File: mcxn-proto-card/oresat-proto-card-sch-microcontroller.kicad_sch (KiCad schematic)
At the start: 102 parts, among them J9 SM14B-SHLS-TF, U1 MCXN947VKLT, U8 TCAN330, Y2 24 MHz

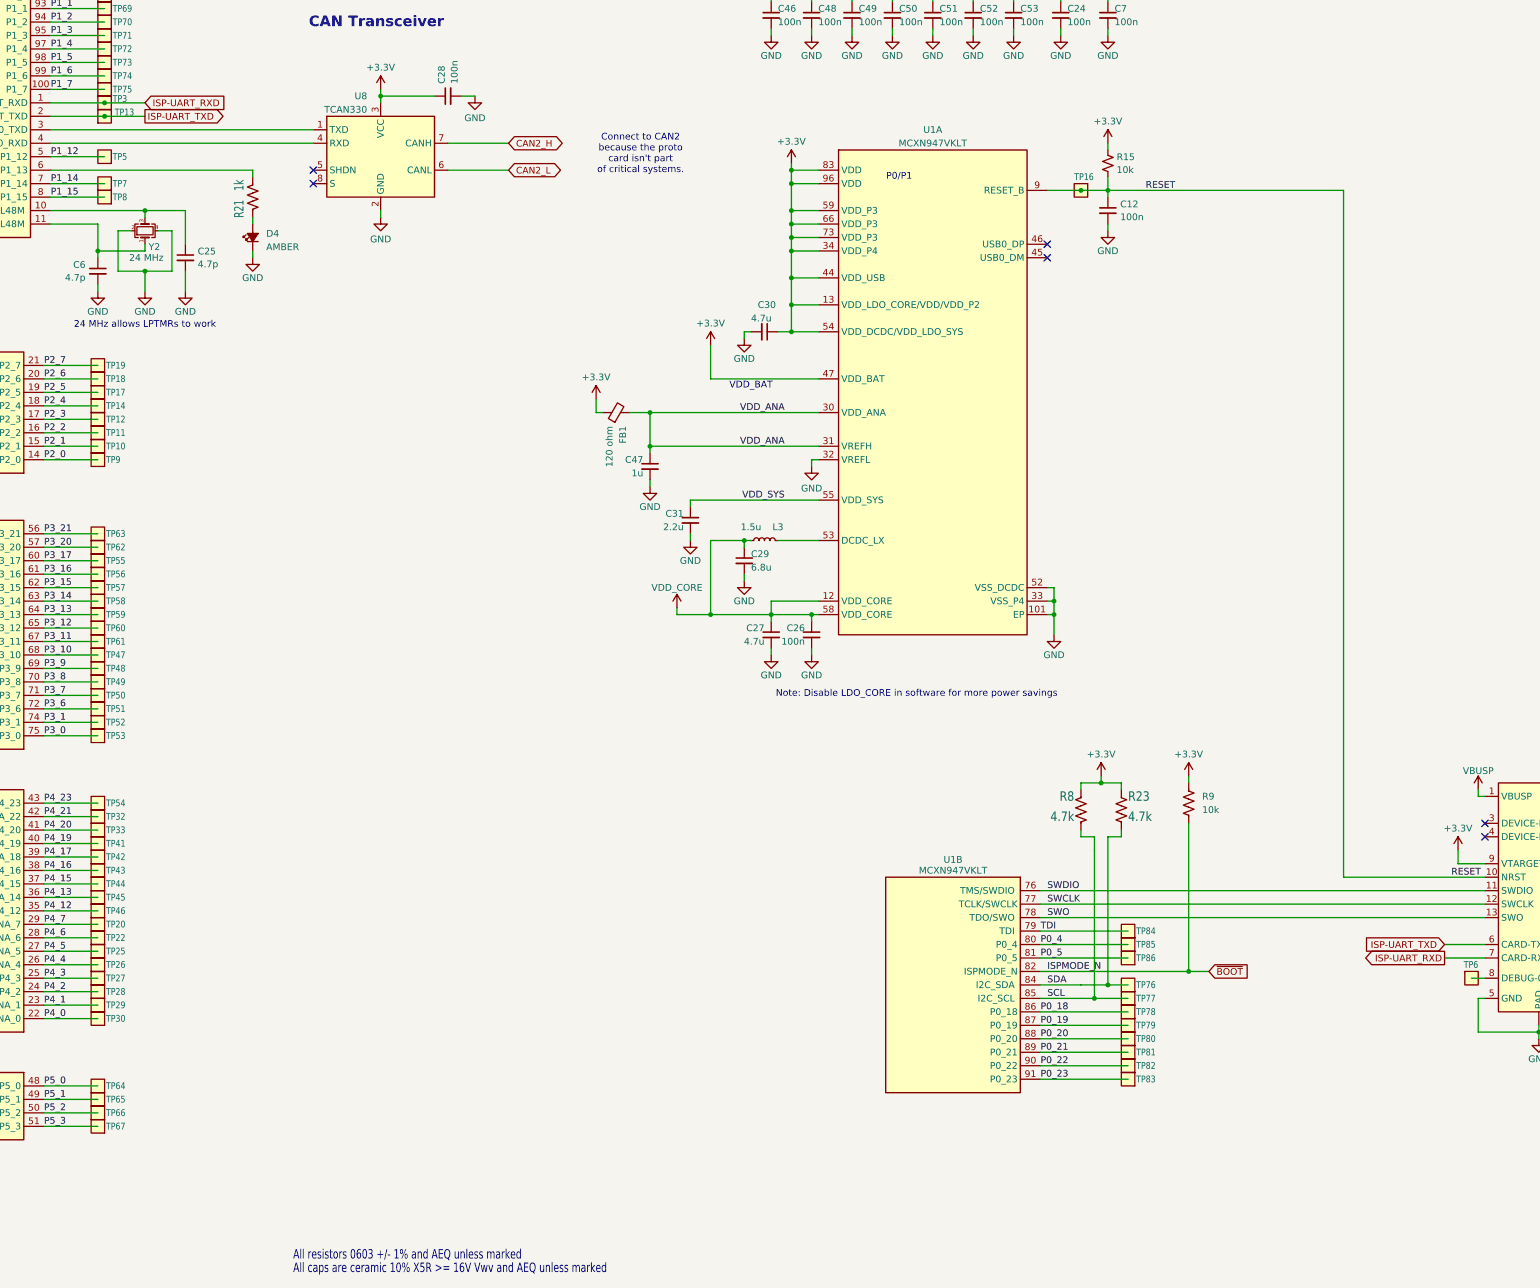
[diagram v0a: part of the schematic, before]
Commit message: Final MCXN protocard cleanup
Made schematic fancy with hierarchical pins, cleaned up schematics a bit, and fixed silk screen a ton. Ready for fab.
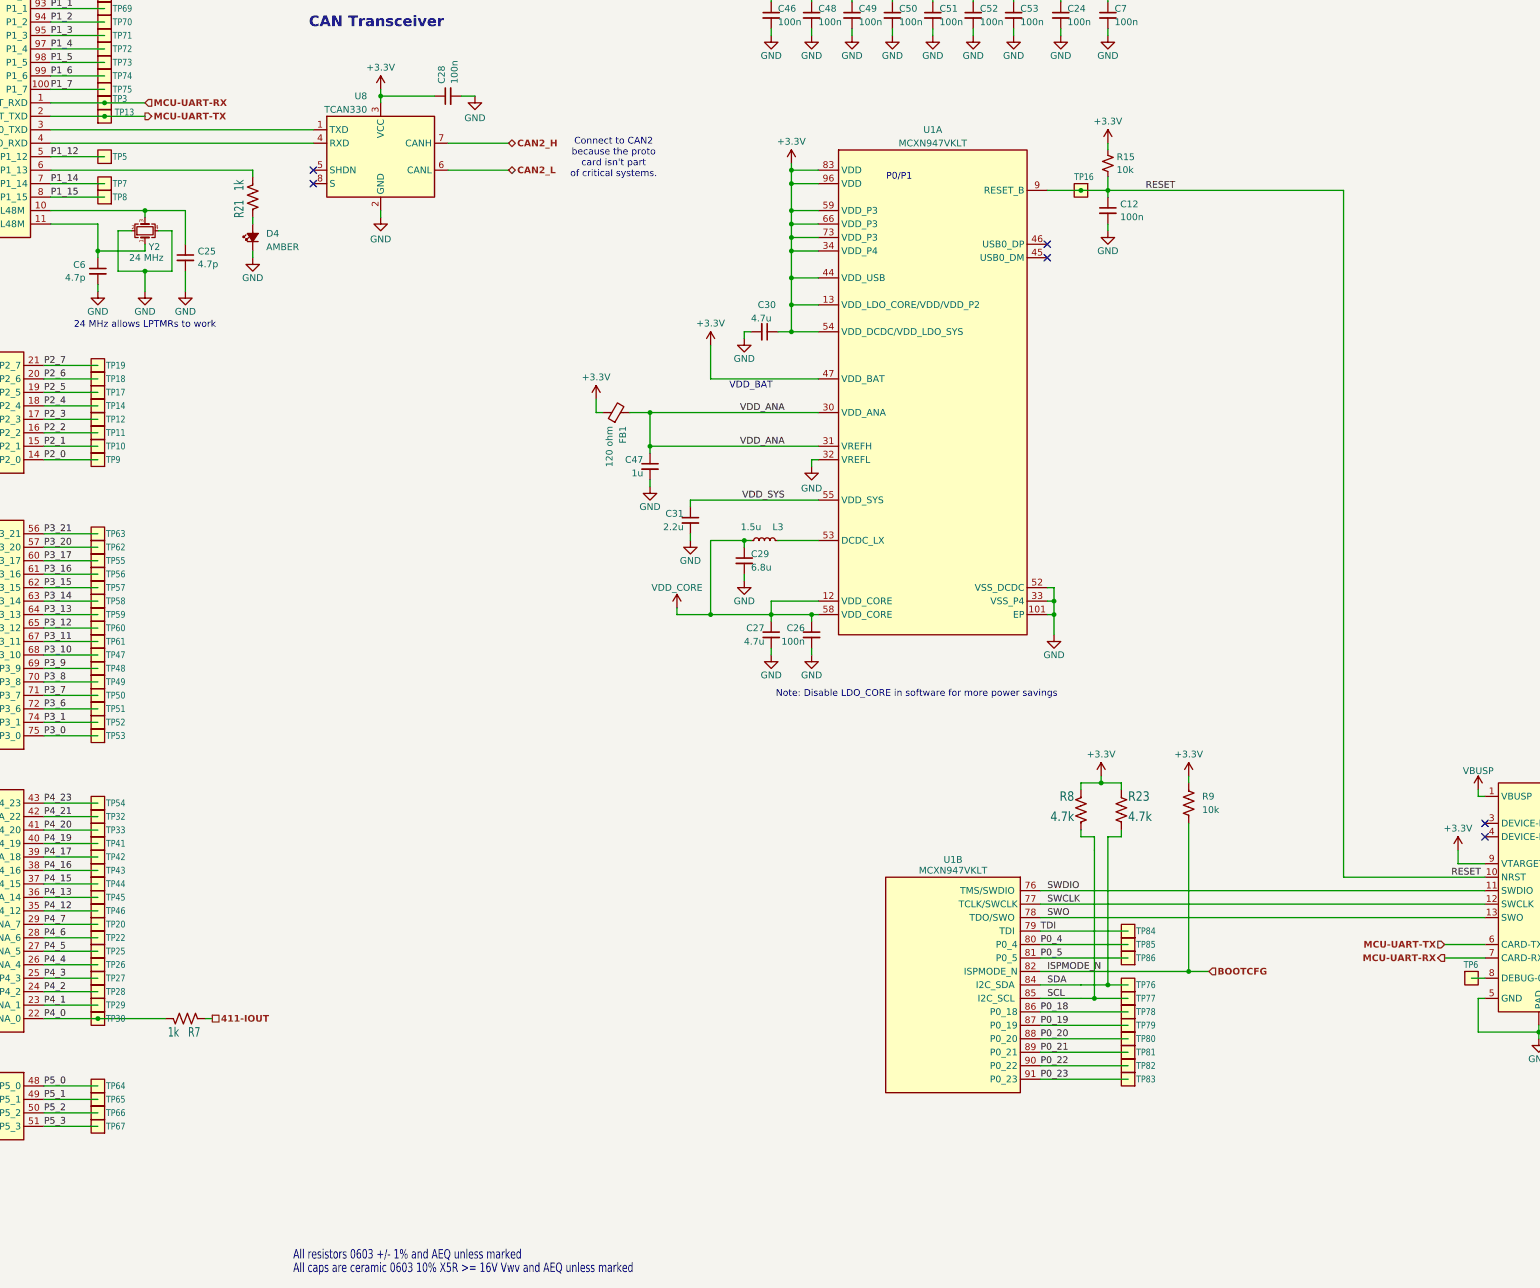
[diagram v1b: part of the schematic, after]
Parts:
- added R7: 1k, oresat-passives:0603-C-NOSILK, symbol Device:R_US
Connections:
- net P4_0: now also R7.1
- net ISP-UART_RXD renamed MCU-UART-RX
- net ISP-UART_TXD renamed MCU-UART-TX
- net ~{BOOT} renamed BOOTCFG
- new net 411-IOUT: R7.2
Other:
- note added: "All caps are ceramic 0603 10% X5R >= 16V Vwv and AEQ unless marked"
- note removed: "All caps are ceramic 10% X5R >= 16V Vwv and AEQ unless marked"
- company: (none) -> Portland State Aerospace Society
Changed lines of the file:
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@@
 	(title_block
 		(title "OreSat MCXN Proto Card")
-		(date "2025-11-13")
+		(date "2025-12-28")
 		(rev "6.0")
+		(company "Portland State Aerospace Society")
 	)
 	(text "Connect to CAN2 \nbecause the proto\ncard isn't part \nof critical systems."
 		(exclude_from_sim no)
-		(at 178.562 55.372 0)
+		(at 173.482 56.134 0)
 		(effects
 			(font
@@
 		)
 	)
-	(text "All caps are ceramic 10% X5R >= 16V Vwv and AEQ unless marked"
+	(text "All caps are ceramic 0603 10% X5R >= 16V Vwv and AEQ unless marked"
 		(exclude_from_sim no)
 		(at 113.03 266.7 0)
@@
 	)
 	(junction
+		(at 76.2 218.44)
+		(diameter 0)
+		(color 0 0 0 0)
+	)
+	(junction
 		(at 129.54 44.45)
 		(diameter 0)
@@
 	(wire
 		(pts
+			(xy 76.2 218.44) (xy 88.9 218.44)
+		)
+		(stroke
+			(width 0)
+			(type default)
+		)
+	)
+	(wire
+		(pts
 			(xy 269.24 173.99) (xy 265.43 173.99)
 		)
@@
 		)
 	)
+	(wire
+		(pts
+			(xy 96.52 218.44) (xy 97.79 218.44)
+		)
+		(stroke
+			(width 0)
+			(type default)
+		)
+	)
 	(label "P3_13"
 		(at 66.04 142.24 0)
@@
 		)
 	)
-	(global_label "ISP-UART_TXD"
-		(shape output)
-		(at 85.09 48.26 0)
-		(fields_autoplaced yes)
+	(hierarchical_label "BOOTCFG"
+		(shape input)
+		(at 285.75 209.55 0)
 		(effects
 			(font
 				(size 1.27 1.27)
+				(thickness 0.254)
+				(bold yes)
 			)
 			(justify left)
 		)
-		(property "Intersheetrefs" "${INTERSHEET_REFS}"
-			(at 101.8033 48.26 0)
-			(effects
-				(font
-					(size 1.27 1.27)
-				)
-				(justify left)
-			)
-		)
 	)
-	(global_label "CAN2_L"
-		(shape bidirectional)
-		(at 153.67 58.42 0)
-		(fields_autoplaced yes)
+	(hierarchical_label "MCU-UART-TX"
+		(shape output)
+		(at 85.09 48.26 0)
 		(effects
 			(font
-				(size 1.2446 1.2446)
+				(size 1.27 1.27)
+				(thickness 0.254)
+				(bold yes)
 			)
 			(justify left)
 		)
-		(property "Intersheetrefs" "${INTERSHEET_REFS}"
-			(at 164.4406 58.42 0)
-			(effects
-				(font
-					(size 1.27 1.27)
-				)
-				(justify left)
-			)
-		)
 	)
-	(global_label "ISP-UART_TXD"
-		(shape input)
-		(at 330.2 204.47 180)
-		(fields_autoplaced yes)
+	(hierarchical_label "CAN2_L"
+		(shape bidirectional)
+		(at 153.67 58.42 0)
 		(effects
 			(font
 				(size 1.27 1.27)
+				(thickness 0.254)
+				(bold yes)
 			)
-			(justify right)
-		)
-		(property "Intersheetrefs" "${INTERSHEET_REFS}"
-			(at 313.4867 204.47 0)
-			(effects
-				(font
-					(size 1.27 1.27)
-				)
-				(justify right)
-			)
+			(justify left)
 		)
 	)
-	(global_label "~{BOOT}"
-		(shape input)
-		(at 285.75 209.55 0)
-		(fields_autoplaced yes)
+	(hierarchical_label "CAN2_H"
+		(shape bidirectional)
+		(at 153.67 53.34 0)
 		(effects
 			(font
 				(size 1.27 1.27)
+				(thickness 0.254)
+				(bold yes)
 			)
 			(justify left)
 		)
-		(property "Intersheetrefs" "${INTERSHEET_REFS}"
-			(at 293.6338 209.55 0)
-			(effects
-				(font
-					(size 1.27 1.27)
-				)
-				(justify left)
-			)
-		)
 	)
-	(global_label "ISP-UART_RXD"
+	(hierarchical_label "MCU-UART-RX"
 		(shape input)
 		(at 85.09 45.72 0)
-		(fields_autoplaced yes)
 		(effects
 			(font
 				(size 1.27 1.27)
+				(thickness 0.254)
+				(bold yes)
 			)
 			(justify left)
 		)
-		(property "Intersheetrefs" "${INTERSHEET_REFS}"
-			(at 102.1057 45.72 0)
-			(effects
-				(font
-					(size 1.27 1.27)
-				)
-				(justify left)
-			)
-		)
 	)
-	(global_label "ISP-UART_RXD"
-		(shape output)
-		(at 330.2 207.01 180)
-		(fields_autoplaced yes)
+	(hierarchical_label "MCU-UART-TX"
+		(shape input)
+		(at 330.2 204.47 180)
 		(effects
 			(font
 				(size 1.27 1.27)
+				(thickness 0.254)
+				(bold yes)
 			)
 			(justify right)
 		)
-		(property "Intersheetrefs" "${INTERSHEET_REFS}"
-			(at 313.1843 207.01 0)
-			(effects
-				(font
-					(size 1.27 1.27)
-				)
-				(justify right)
-			)
-		)
 	)
-	(global_label "CAN2_H"
-		(shape bidirectional)
-		(at 153.67 53.34 0)
-		(fields_autoplaced yes)
+	(hierarchical_label "411-IOUT"
+		(shape passive)
+		(at 97.79 218.44 0)
 		(effects
 			(font
-				(size 1.2446 1.2446)
+				(size 1.27 1.27)
+				(thickness 0.254)
+				(bold yes)
 			)
 			(justify left)
 		)
-		(property "Intersheetrefs" "${INTERSHEET_REFS}"
-			(at 164.737 53.34 0)
-			(effects
-				(font
-					(size 1.27 1.27)
-				)
-				(justify left)
+	)
+	(hierarchical_label "MCU-UART-RX"
+		(shape output)
+		(at 330.2 207.01 180)
+		(effects
+			(font
+				(size 1.27 1.27)
+				(thickness 0.254)
+				(bold yes)
 			)
+			(justify right)
 		)
 	)
@@
 					(unit 1)
 				)
+			)
+		)
+	)
+	(symbol
+		(lib_id "Device:R_US")
+		(at 92.71 218.44 90)
+		(mirror x)
+		(unit 1)
+		(exclude_from_sim no)
+		(in_bom yes)
+		(on_board yes)
+		(dnp no)
+		(property "Reference" "R7"
+			(at 93.218 219.964 90)
+			(effects
+				(font
+					(size 1.778 1.27)
+				)
+				(justify right top)
+			)
+		)
+		(property "Value" "1k"
+			(at 89.408 219.964 90)
+			(effects
+				(font
+					(size 1.778 1.27)
+				)
+				(justify right top)
+			)
+		)
+		(property "Footprint" "oresat-passives:0603-C-NOSILK"
+			(at 92.964 219.456 90)
+			(effects
+				(font
+					(size 1.27 1.27)
+				)
+				(hide yes)
+			)
+		)
+		(property "Datasheet" "https://www.seielect.com/catalog/sei-rmcf_rmcp.pdf"
+			(at 92.71 218.44 0)
+			(effects
+				(font
+					(size 1.27 1.27)
+				)
+				(hide yes)
+			)
+		)
+		(property "Description" ""
+			(at 92.71 218.44 0)
+			(effects
+				(font
+					(size 1.27 1.27)
+				)
+				(hide yes)
+			)
+		)
+		(property "DIS" "Digi-Key"
+			(at 92.71 218.44 0)
+			(effects
+				(font
+					(size 1.27 1.27)
+				)
+				(justify left bottom)
+				(hide yes)
+			)
+		)
+		(property "DPN" ""
+			(at 92.71 218.44 0)
+			(effects
+				(font
+					(size 1.27 1.27)
+				)
+				(justify left bottom)
+				(hide yes)
+			)
+		)
+		(property "MFR" "Stackpole Electronics Inc"
+			(at 92.71 218.44 0)
+			(effects
+				(font
+					(size 1.27 1.27)
+				)
+				(justify left bottom)
+				(hide yes)
+			)
+		)
+		(property "MPN" ""
+			(at 92.71 218.44 0)
+			(effects
+				(font
+					(size 1.27 1.27)
+				)
+				(justify left bottom)
+				(hide yes)
+			)
+		)
+		(pin "1"
+		)
+		(pin "2"
+		)
+		(instances
+			(project "oresat-proto-card"
+				(path "/04d32576-d084-475b-9eac-d7f3fd9579d7/e68cb6cd-039d-43ad-93aa-b705d581519b"
+					(reference "R7")
+					(unit 1)
+				)

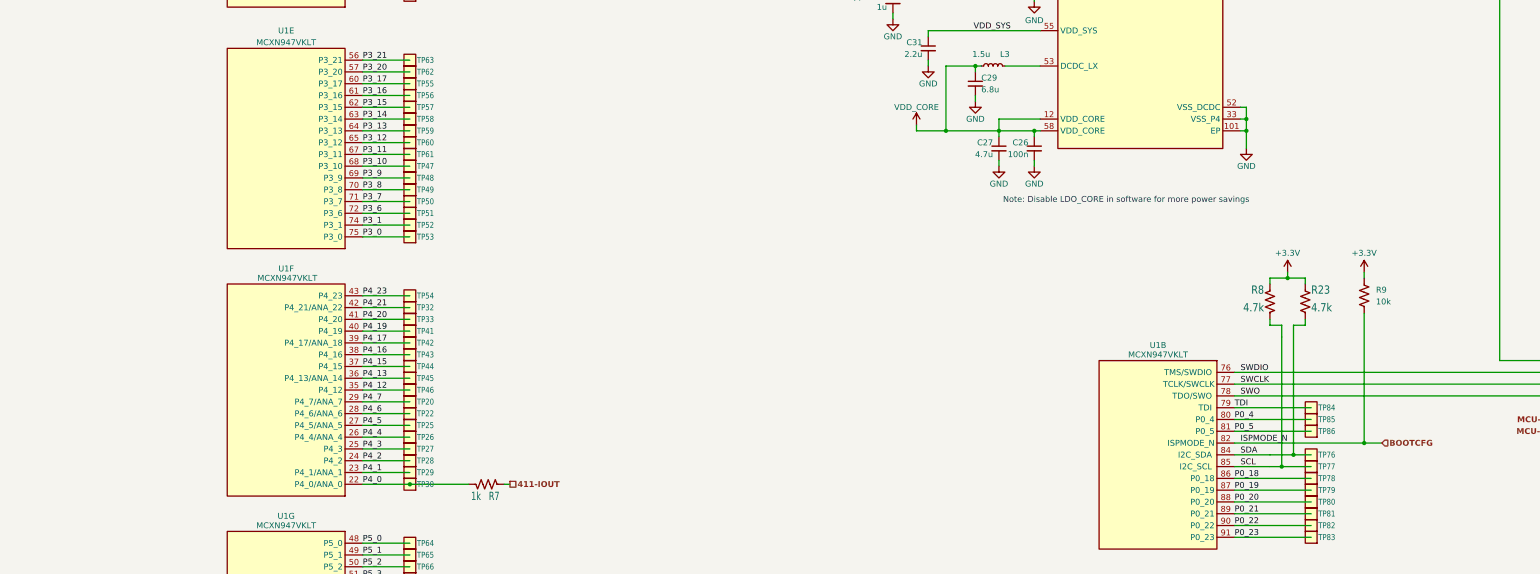
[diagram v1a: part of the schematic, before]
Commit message: BOM fixed; schematic polish (no change to PCB v6.0)
Fixed BOM, and synced with OreSat BOMs Google Sheet. Figured out large capacitor (> 4.7u) voltages and package issues, which are many. Set MCXN pin names to the right selection if possible.
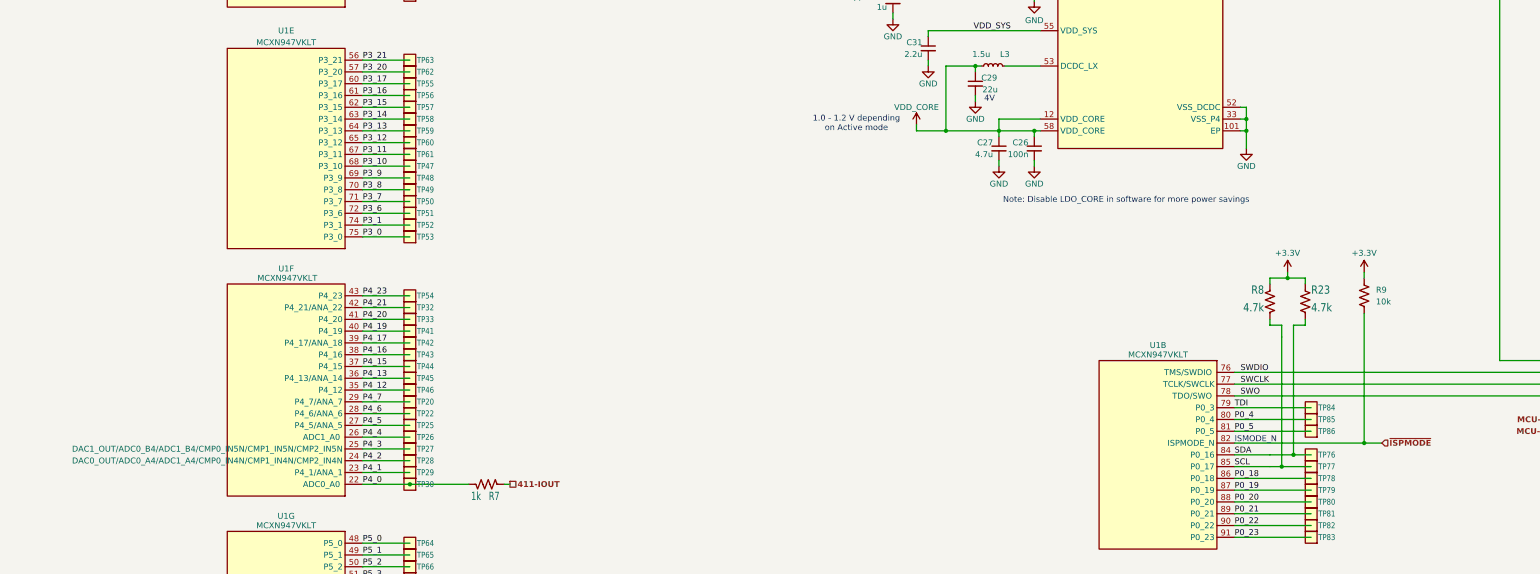
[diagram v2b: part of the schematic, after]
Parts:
- C12, C24, C26, C28, C46, C48, C49, C50, C51, C52, C53, C7: DPN 587-3472-1-ND -> 399-6856-1-ND; MFR Taiyo Yuden -> KEMET; MPN TMK107BJ104KAHT -> C0603C104K5RACAUTO
- C25, C6: DPN 490-GRM1885C1H4R7WA01DCT-ND -> 399-15924-1-ND; MFR Murata -> KEMET; MPN GRM1885C1H4R7WA01D -> C0603C479D5GACAUTO
- C29: value 6.8u -> 22u; DPN 445-12661-1-ND -> 478-KAM15CT70G226KTCT-ND; MFR TDK Corporation -> KYOCERA AVX; MPN CGA4J1X5R1C685K125AC -> KAM15CT70G226KT
- C31: DPN 587-4929-1-ND -> 490-GRT188C71E225KE13DCT-ND; MFR Taiyo Yuden -> Murata Electronics; MPN TMK107BBJ225MAHT -> GRT188C71E225KE13D
- C47: DPN 587-3473-1-ND -> 490-GRT188R71E105KE13DCT-ND; MFR Taiyo Yuden -> Murata Electronics; MPN TMK107BJ105KAHT -> GRT188R71E105KE13D
- FB1, L3, R23, R8, Y2: DIS DIgiKey -> DigiKey
- R21, R7: DIS Digi-Key -> DigiKey; DPN (none) -> RMCF0603FT1K00CT-ND; MPN (none) -> RMCF0603FT1K00
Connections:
- net BOOTCFG renamed ~{ISPMODE}
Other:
- note added: "1.0 - 1.2 V depending on Active mode"
- note added: "4V"
- note added: "ISMODE_N"
- moved on the sheet: U1F
